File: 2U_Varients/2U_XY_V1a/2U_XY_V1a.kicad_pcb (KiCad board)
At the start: 4 copper layers, 83 x 212.6 mm, 28 parts, among them CN1 DF11-2DSA-4DP, J2 Conn_01x01, J3 Conn_01x01, J4 Conn_01x01, J5 Conn_01x01, U2 TMP112xxDRL, U3 DRV2605LDGS, U4 TCA4311ADGKR, U5 5040500691, U7 VEML6031X00

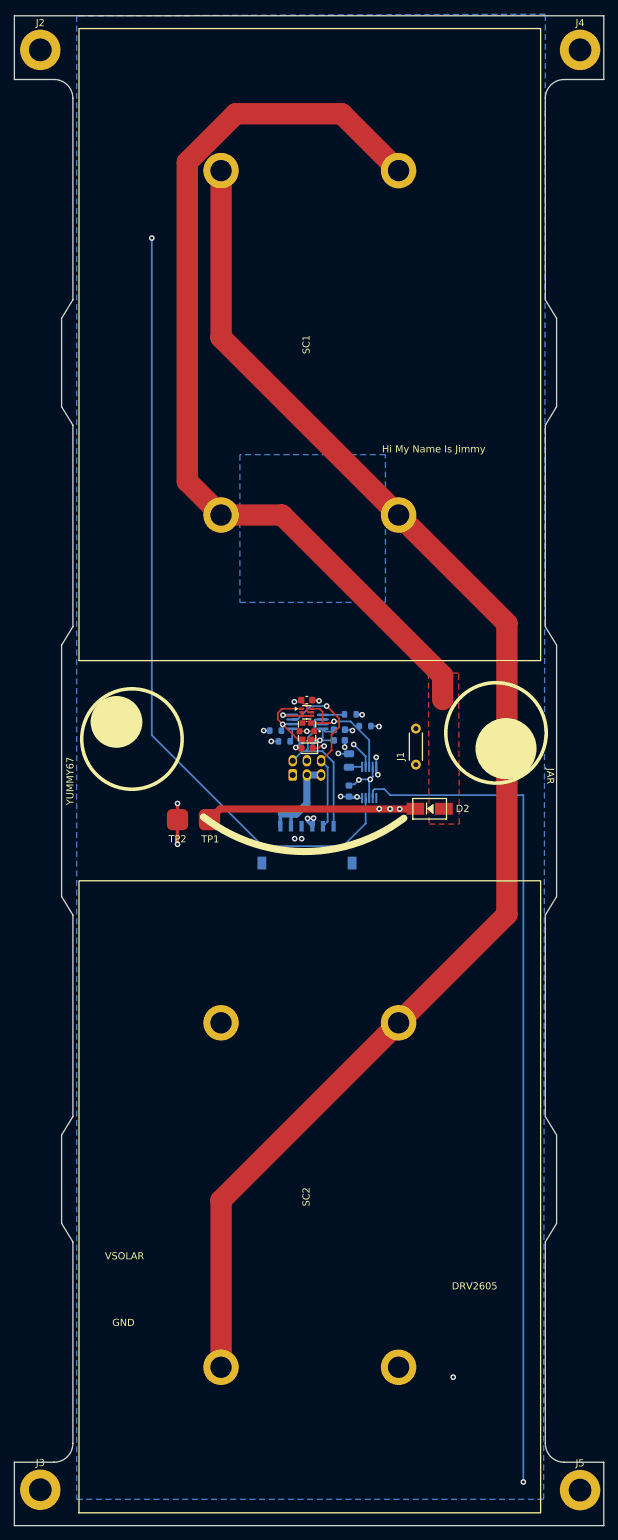
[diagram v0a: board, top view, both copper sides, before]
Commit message: Coil and Fastener Cutout
Rerouted Coil and added cutout for fasteners
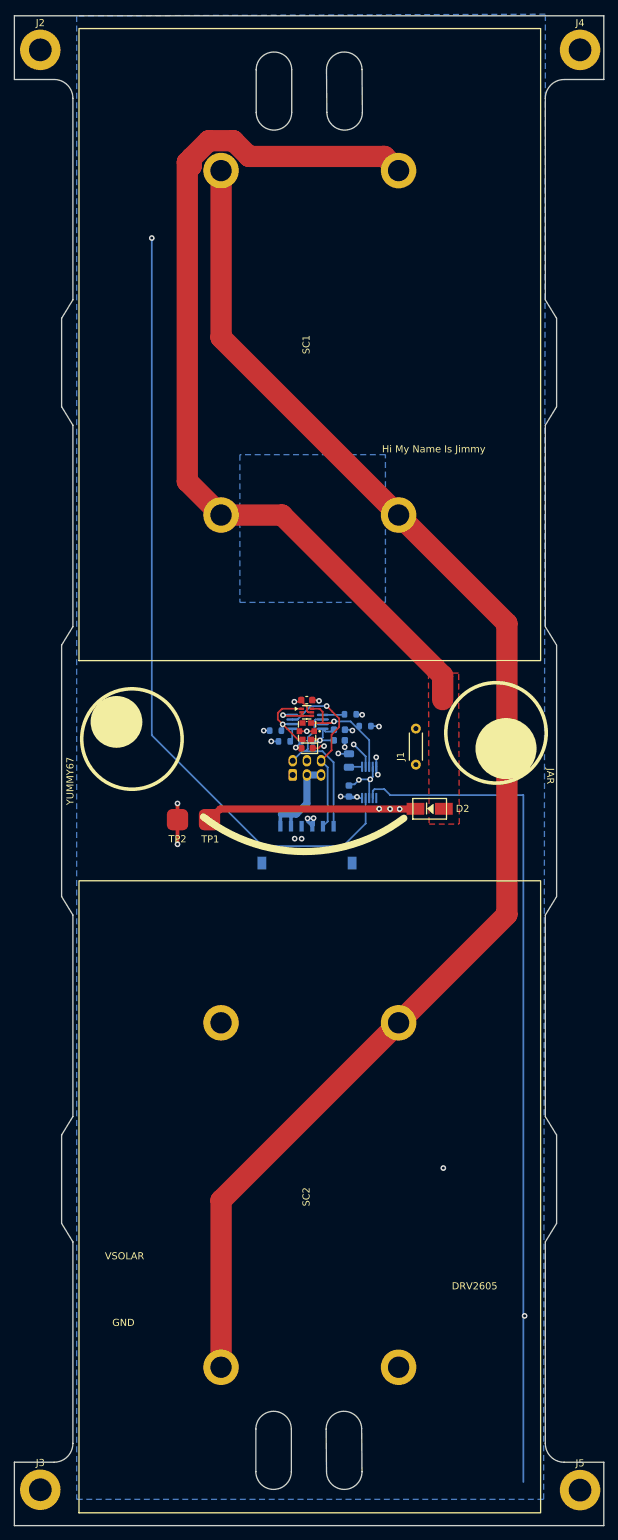
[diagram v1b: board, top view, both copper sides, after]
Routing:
- net Net-(U3-OUT+): track 20577.9 -> 18357.9 mm
- net /SOL_OUT: track 131.5 -> 129.4 mm
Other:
- outline, holes or cut-outs redrawn
